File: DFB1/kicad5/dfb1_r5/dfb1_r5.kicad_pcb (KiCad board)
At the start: 4 copper layers, 169 x 71.4 mm, 79 parts, among them IC1 IS42S16320D-7TL, IC2 IS42S16320D-7TL, IC3 SN74CB3T3245PW, IC4 SN74CB3T3245PW, IC5 SN74CB3T3245PW, IC6 SN74CB3T3245PW, J1 Conn_01x50, J2 Conn_02x04_Odd_Even, J3 Conn_01x30, J4 Conn_02x03_Odd_Even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

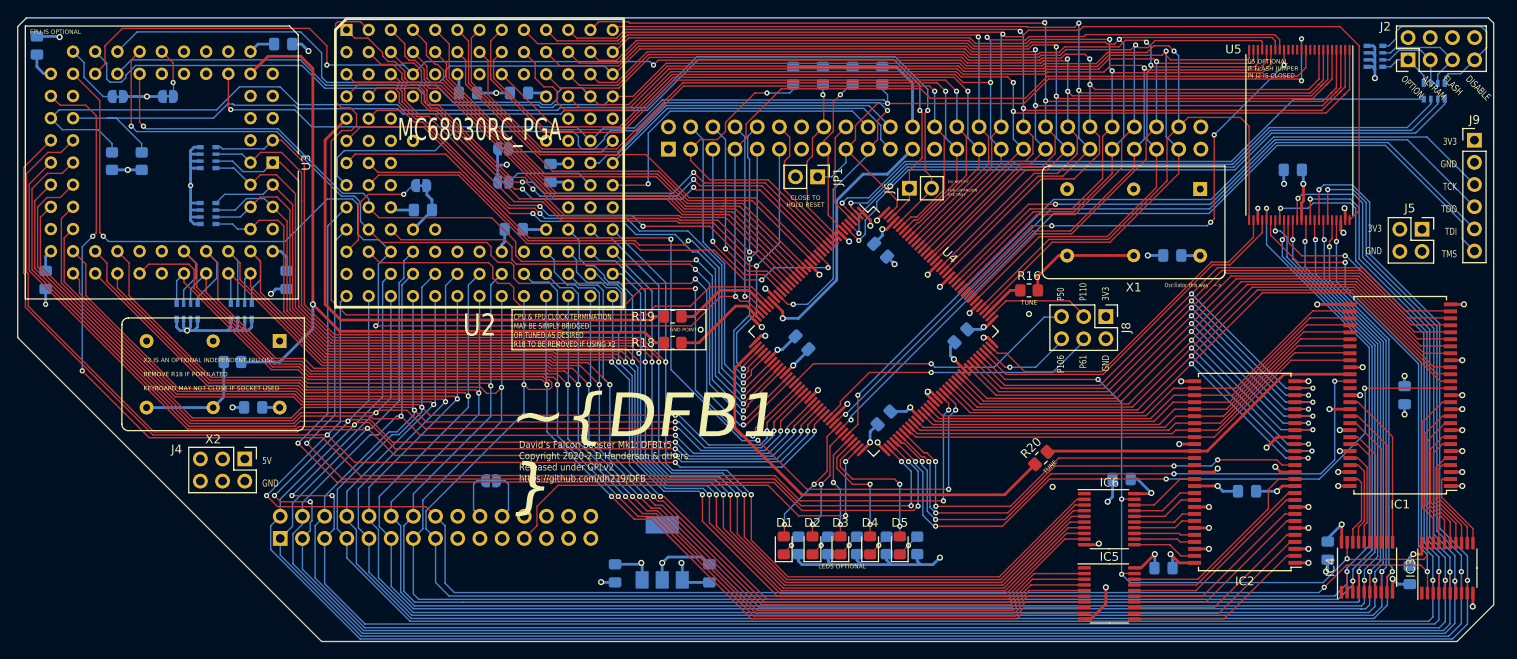
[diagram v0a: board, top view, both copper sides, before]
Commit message: rework for pcbway tolerances and cleanup
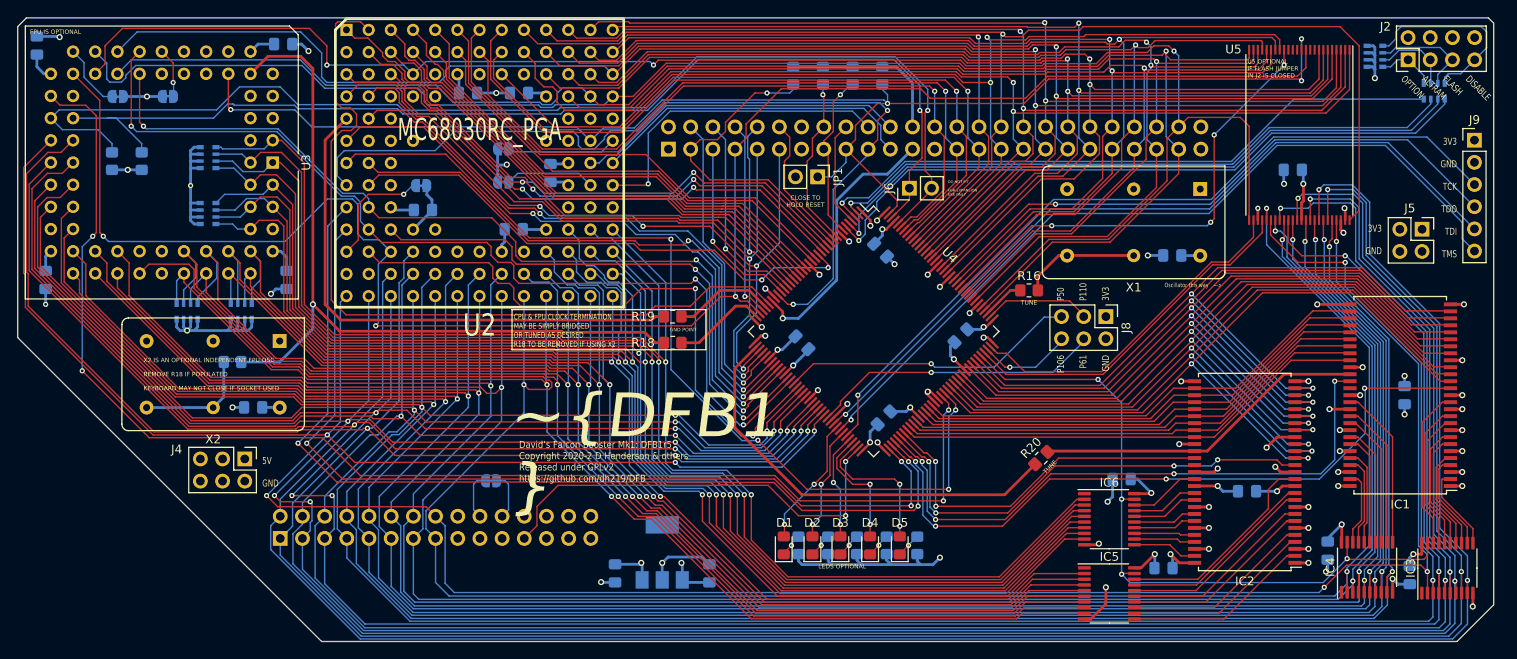
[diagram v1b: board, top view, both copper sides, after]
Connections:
- net /~EXPD renamed /~{EXPD}
- net /~IACK renamed /~{IACK}
- net /~MFP_IEI renamed /~{MFP_IEI}
- net /~MFP_INT renamed /~{MFP_INT}
- net /~XINT1 renamed /~{XINT1}
- net /~XINT3 renamed /~{XINT3}
- net XR~W renamed XR~{W}
- net ~AS renamed ~{AS}
- net ~AVEC renamed ~{AVEC}
- net ~BERR renamed ~{BERR}
- net ~BG renamed ~{BG}
- net ~BGK renamed ~{BGK}
- net ~BOE renamed ~{BOE}
- net ~BR renamed ~{BR}
- net ~CAS renamed ~{CAS}
- net ~CBACK renamed ~{CBACK}
- net ~CBREQ renamed ~{CBREQ}
- net ~DS renamed ~{DS}
- net ~DSACK0 renamed ~{DSACK0}
- net ~DSACK1 renamed ~{DSACK1}
- net ~FPUCS renamed ~{FPUCS}
- net ~FPUDSACK0 renamed ~{FPUDSACK0}
- net ~FPUDSACK1 renamed ~{FPUDSACK1}
- net ~HLT renamed ~{HLT}
- net ~IPL0 renamed ~{IPL0}
- net ~IPL1 renamed ~{IPL1}
- net ~IPL2 renamed ~{IPL2}
- net ~LDS renamed ~{LDS}
- net ~RAMWE renamed ~{RAMWE}
- net ~RAS renamed ~{RAS}
- net ~ROMCE renamed ~{ROMCE}
- net ~ROMOE renamed ~{ROMOE}
- net ~RST renamed ~{RST}
- net ~STERM renamed ~{STERM}
- net ~UDS renamed ~{UDS}
- net ~XAS renamed ~{XAS}
- net ~XBG renamed ~{XBG}
- net ~XBGK renamed ~{XBGK}
- net ~XBR renamed ~{XBR}
- net ~XDTACK renamed ~{XDTACK}
- net ~XHALT renamed ~{XHALT}
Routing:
- net D3: track 152.2 -> 151.1 mm
- net A18: track 125.9 -> 125.0 mm
- net ~{HLT}: track 61.4 -> 60.6 mm
- net GND: vias 52 -> 49
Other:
- net class CLK removed
- net class Default removed
- net class PWR removed
- board text added: "~{DFB1 }"
- board text removed: "~DFB1"

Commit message: fix logo
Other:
- board text added: "~{DFB1}"
- board text removed: "~{DFB1 }"
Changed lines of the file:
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@@
     (effects (font (size 0.5 0.5) (thickness 0.1)))
   )
-  (gr_text "~{DFB1\n}           " (at 107.2 94.2) (layer "F.SilkS")
+  (gr_text "~{DFB1}" (at 107.188 90.043) (layer "F.SilkS")
     (effects (font (size 5 5.45) (thickness 1) italic) (justify left))
   )
